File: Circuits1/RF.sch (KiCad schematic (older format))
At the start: 16 parts

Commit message: PCB Layout with 0806
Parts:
- removed X?: QUARTZCMS4, ~, symbol QUARTZCMS4
- added X2: QUARTZ, ~, symbol QUARTZ
- gave numbers to parts that had none: 15
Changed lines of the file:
@@
 LIBS:ATMEGA32U4
 LIBS:nRF24L01+
+LIBS:LD1117
+LIBS:MPU-6050
 LIBS:Rx-cache
 EELAYER 27 0
@@
 $Descr A4 11693 8268
 encoding utf-8
-Sheet 2 2
+Sheet 2 3
 Title "noname.sch"
-Date "16 dec 2013"
+Date "22 dec 2013"
 Rev ""
 Comp ""
@@
 $EndDescr
 $Comp
-L NRF24L01+ U?
+L NRF24L01+ U3
 U 1 1 52AF7B40
 P 5550 3550
-F 0 "U?" H 5550 3450 50  0000 C CNN
+F 0 "U3" H 5550 3450 50  0000 C CNN
 F 1 "NRF24L01+" H 5550 3650 50  0000 C CNN
 F 2 "MODULE" H 5550 3550 50  0001 C CNN
@@
 $EndComp
 $Comp
-L C C?
+L C C13
 U 1 1 52AF7B4F
 P 4300 2050
-F 0 "C?" H 4300 2150 40  0000 L CNN
+F 0 "C13" H 4300 2150 40  0000 L CNN
 F 1 "10nF" H 4306 1965 40  0000 L CNN
 F 2 "~" H 4338 1900 30  0000 C CNN
@@
 $EndComp
 $Comp
-L 3V3 #PWR?
+L 3V3 #PWR039
 U 1 1 52AF7B9D
 P 4400 2850
-F 0 "#PWR?" H 4400 2950 40  0001 C CNN
+F 0 "#PWR039" H 4400 2950 40  0001 C CNN
 F 1 "3V3" H 4400 2975 40  0000 C CNN
 F 2 "" H 4400 2850 60  0000 C CNN
@@
 $EndComp
 $Comp
-L 3V3 #PWR?
+L 3V3 #PWR040
 U 1 1 52AF7BC7
 P 4400 3300
-F 0 "#PWR?" H 4400 3400 40  0001 C CNN
+F 0 "#PWR040" H 4400 3400 40  0001 C CNN
 F 1 "3V3" H 4400 3425 40  0000 C CNN
 F 2 "" H 4400 3300 60  0000 C CNN
@@
 $EndComp
 $Comp
-L 3V3 #PWR?
+L 3V3 #PWR041
 U 1 1 52AF7BCD
 P 4400 3900
-F 0 "#PWR?" H 4400 4000 40  0001 C CNN
+F 0 "#PWR041" H 4400 4000 40  0001 C CNN
 F 1 "3V3" H 4400 4025 40  0000 C CNN
 F 2 "" H 4400 3900 60  0000 C CNN
@@
 $EndComp
 $Comp
-L GND #PWR?
+L GND #PWR042
 U 1 1 52AF7BF4
 P 4400 4250
-F 0 "#PWR?" H 4400 4250 30  0001 C CNN
+F 0 "#PWR042" H 4400 4250 30  0001 C CNN
 F 1 "GND" H 4400 4180 30  0001 C CNN
 F 2 "" H 4400 4250 60  0000 C CNN
@@
 $EndComp
 $Comp
-L GND #PWR?
+L GND #PWR043
 U 1 1 52AF7C01
 P 4400 3800
-F 0 "#PWR?" H 4400 3800 30  0001 C CNN
+F 0 "#PWR043" H 4400 3800 30  0001 C CNN
 F 1 "GND" H 4400 3730 30  0001 C CNN
 F 2 "" H 4400 3800 60  0000 C CNN
@@
 $EndComp
 $Comp
-L GND #PWR?
+L GND #PWR044
 U 1 1 52AF7C07
 P 4400 3200
-F 0 "#PWR?" H 4400 3200 30  0001 C CNN
+F 0 "#PWR044" H 4400 3200 30  0001 C CNN
 F 1 "GND" H 4400 3130 30  0001 C CNN
 F 2 "" H 4400 3200 60  0000 C CNN
@@
 $EndComp
 $Comp
-L GND #PWR?
+L GND #PWR045
 U 1 1 52AF7C0D
 P 4400 2950
-F 0 "#PWR?" H 4400 2950 30  0001 C CNN
+F 0 "#PWR045" H 4400 2950 30  0001 C CNN
 F 1 "GND" H 4400 2880 30  0001 C CNN
 F 2 "" H 4400 2950 60  0000 C CNN
@@
 $EndComp
 $Comp
-L R R?
+L R R8
 U 1 1 52AF7C2F
 P 4250 3550
-F 0 "R?" V 4330 3550 40  0000 C CNN
+F 0 "R8" V 4330 3550 40  0000 C CNN
 F 1 "22K" V 4257 3551 40  0000 C CNN
 F 2 "~" V 4180 3550 30  0000 C CNN
@@
 $EndComp
 $Comp
-L GND #PWR?
+L GND #PWR046
 U 1 1 52AF7C69
 P 3900 3550
-F 0 "#PWR?" H 3900 3550 30  0001 C CNN
+F 0 "#PWR046" H 3900 3550 30  0001 C CNN
 F 1 "GND" H 3900 3480 30  0001 C CNN
 F 2 "" H 3900 3550 60  0000 C CNN
@@
 $EndComp
 $Comp
-L C C?
+L C C14
 U 1 1 52AF7CD7
 P 4600 2050
-F 0 "C?" H 4600 2150 40  0000 L CNN
+F 0 "C14" H 4600 2150 40  0000 L CNN
 F 1 "1nF" H 4606 1965 40  0000 L CNN
 F 2 "~" H 4638 1900 30  0000 C CNN
@@
 $EndComp
 $Comp
-L 3V3 #PWR?
+L 3V3 #PWR047
 U 1 1 52AF7CEB
 P 4450 1700
-F 0 "#PWR?" H 4450 1800 40  0001 C CNN
+F 0 "#PWR047" H 4450 1800 40  0001 C CNN
 F 1 "3V3" H 4450 1825 40  0000 C CNN
 F 2 "" H 4450 1700 60  0000 C CNN
@@
 $EndComp
 $Comp
-L GND #PWR?
+L GND #PWR048
 U 1 1 52AF7D51
 P 4450 2350
-F 0 "#PWR?" H 4450 2350 30  0001 C CNN
+F 0 "#PWR048" H 4450 2350 30  0001 C CNN
 F 1 "GND" H 4450 2280 30  0001 C CNN
 F 2 "" H 4450 2350 60  0000 C CNN
@@
 3V3
 $Comp
-L QUARTZCMS4 X?
-U 1 1 52AF7E4F
-P 7250 3700
-F 0 "X?" H 7250 3850 60  0000 C CNN
-F 1 "QUARTZCMS4" H 7250 3550 60  0000 C CNN
-F 2 "~" H 7250 3700 60  0000 C CNN
-F 3 "~" H 7250 3700 60  0000 C CNN
-	1    7250 3700
-	0    -1   -1   0
-$EndComp
-$Comp
-L R R?
+L R R9
 U 1 1 52AF7E5E
 P 7600 3700
-F 0 "R?" V 7680 3700 40  0000 C CNN
+F 0 "R9" V 7680 3700 40  0000 C CNN
 F 1 "1M" V 7607 3701 40  0000 C CNN
 F 2 "~" V 7530 3700 30  0000 C CNN
@@
 $EndComp
 $Comp
-L C C?
+L C C16
 U 1 1 52AF7E77
 P 8000 3400
-F 0 "C?" H 8000 3500 40  0000 L CNN
+F 0 "C16" H 8000 3500 40  0000 L CNN
 F 1 "22pF" H 8006 3315 40  0000 L CNN
 F 2 "~" H 8038 3250 30  0000 C CNN
@@
 $EndComp
 $Comp
-L C C?
+L C C17
 U 1 1 52AF7E9C
 P 8000 4000
-F 0 "C?" H 8000 4100 40  0000 L CNN
+F 0 "C17" H 8000 4100 40  0000 L CNN
 F 1 "22pF" H 8006 3915 40  0000 L CNN
 F 2 "~" H 8038 3850 30  0000 C CNN
@@
 $EndComp
 $Comp
-L GND #PWR?
+L GND #PWR049
 U 1 1 52AF7F50
 P 8300 3400
-F 0 "#PWR?" H 8300 3400 30  0001 C CNN
+F 0 "#PWR049" H 8300 3400 30  0001 C CNN
 F 1 "GND" H 8300 3330 30  0001 C CNN
 F 2 "" H 8300 3400 60  0000 C CNN
@@
 $EndComp
 $Comp
-L GND #PWR?
+L GND #PWR050
 U 1 1 52AF7F6A
 P 8300 4000
-F 0 "#PWR?" H 8300 4000 30  0001 C CNN
+F 0 "#PWR050" H 8300 4000 30  0001 C CNN
 F 1 "GND" H 8300 3930 30  0001 C CNN
 F 2 "" H 8300 4000 60  0000 C CNN
@@
 $EndComp
 $Comp
-L INDUCTOR_SMALL L?
+L INDUCTOR_SMALL L1
 U 1 1 52AF7FBE
 P 6650 4600
-F 0 "L?" H 6650 4700 50  0000 C CNN
+F 0 "L1" H 6650 4700 50  0000 C CNN
 F 1 "8.2nH" H 6650 4550 50  0000 C CNN
 F 2 "~" H 6650 4600 60  0000 C CNN
@@
 $EndComp
 $Comp
-L INDUCTOR_SMALL L?
+L INDUCTOR_SMALL L2
 U 1 1 52AF7FDC
 P 7200 4850
-F 0 "L?" H 7200 4950 50  0000 C CNN
+F 0 "L2" H 7200 4950 50  0000 C CNN
 F 1 "3.9nH" H 7200 4800 50  0000 C CNN
 F 2 "~" H 7200 4850 60  0000 C CNN
@@
 $EndComp
 $Comp
-L INDUCTOR_SMALL L?
+L INDUCTOR_SMALL L3
 U 1 1 52AF7FEE
 P 7550 4350
-F 0 "L?" H 7550 4450 50  0000 C CNN
+F 0 "L3" H 7550 4450 50  0000 C CNN
 F 1 "2.7nH" H 7550 4300 50  0000 C CNN
 F 2 "~" H 7550 4350 60  0000 C CNN
@@
 $EndComp
 $Comp
-L C C?
+L C C20
 U 1 1 52AF8000
 P 8400 4400
-F 0 "C?" H 8400 4500 40  0000 L CNN
+F 0 "C20" H 8400 4500 40  0000 L CNN
 F 1 "2.2nF" H 8406 4315 40  0000 L CNN
 F 2 "~" H 8438 4250 30  0000 C CNN
@@
 $EndComp
 $Comp
-L C C?
+L C C18
 U 1 1 52AF8021
 P 8200 4400
-F 0 "C?" H 8200 4500 40  0000 L CNN
+F 0 "C18" H 8200 4500 40  0000 L CNN
 F 1 "4.7pF" H 8206 4315 40  0000 L CNN
 F 2 "~" H 8238 4250 30  0000 C CNN
@@
 $EndComp
 $Comp
-L GND #PWR?
+L GND #PWR051
 U 1 1 52AF8065
 P 8200 4700
-F 0 "#PWR?" H 8200 4700 30  0001 C CNN
+F 0 "#PWR051" H 8200 4700 30  0001 C CNN
 F 1 "GND" H 8200 4630 30  0001 C CNN
 F 2 "" H 8200 4700 60  0000 C CNN
@@
 $EndComp
 $Comp
-L GND #PWR?
+L GND #PWR052
 U 1 1 52AF806B
 P 8400 4700
-F 0 "#PWR?" H 8400 4700 30  0001 C CNN
+F 0 "#PWR052" H 8400 4700 30  0001 C CNN
 F 1 "GND" H 8400 4630 30  0001 C CNN
 F 2 "" H 8400 4700 60  0000 C CNN
@@
 $EndComp
 $Comp
-L C C?
+L C C15
 U 1 1 52AF8280
 P 7850 4850
-F 0 "C?" H 7850 4950 40  0000 L CNN
+F 0 "C15" H 7850 4950 40  0000 L CNN
 F 1 "1.5pF" H 7856 4765 40  0000 L CNN
 F 2 "~" H 7888 4700 30  0000 C CNN
@@
 $EndComp
 $Comp
-L C C?
+L C C19
 U 1 1 52AF8292
 P 8250 5050
-F 0 "C?" H 8250 5150 40  0000 L CNN
+F 0 "C19" H 8250 5150 40  0000 L CNN
 F 1 "1pF" H 8256 4965 40  0000 L CNN
 F 2 "~" H 8288 4900 30  0000 C CNN
@@
 $EndComp
 $Comp
-L GND #PWR?
+L GND #PWR053
 U 1 1 52AF8326
 P 8250 5400
-F 0 "#PWR?" H 8250 5400 30  0001 C CNN
+F 0 "#PWR053" H 8250 5400 30  0001 C CNN
 F 1 "GND" H 8250 5330 30  0001 C CNN
 F 2 "" H 8250 5400 60  0000 C CNN
@@
 ANTENNA
 $Comp
-L C C?
+L C C12
 U 1 1 52AF8407
 P 4250 4150
-F 0 "C?" H 4250 4250 40  0000 L CNN
+F 0 "C12" H 4250 4250 40  0000 L CNN
 F 1 "33nF" H 4256 4065 40  0000 L CNN
 F 2 "~" H 4288 4000 30  0000 C CNN
@@
 $EndComp
 $Comp
-L GND #PWR?
+L GND #PWR054
 U 1 1 52AF841C
 P 3950 4150
-F 0 "#PWR?" H 3950 4150 30  0001 C CNN
+F 0 "#PWR054" H 3950 4150 30  0001 C CNN
 F 1 "GND" H 3950 4080 30  0001 C CNN
 F 2 "" H 3950 4150 60  0000 C CNN
@@
 Wire Wire Line
 	4450 4150 4600 4150
+$Comp
+L QUARTZ X2
+U 1 1 52B08D5B
+P 7250 3700
+F 0 "X2" H 7250 3850 60  0000 C CNN
+F 1 "QUARTZ" H 7250 3550 60  0000 C CNN
+F 2 "~" H 7250 3700 60  0000 C CNN
+F 3 "~" H 7250 3700 60  0000 C CNN
+	1    7250 3700
+	0    -1   -1   0
+$EndComp
 $EndSCHEMATC

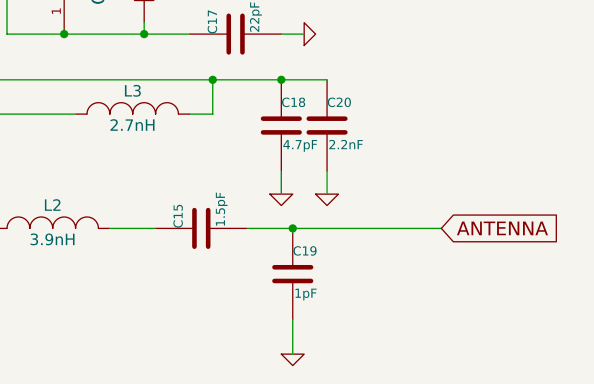
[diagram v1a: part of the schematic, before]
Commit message: Antenna and Ground Planes
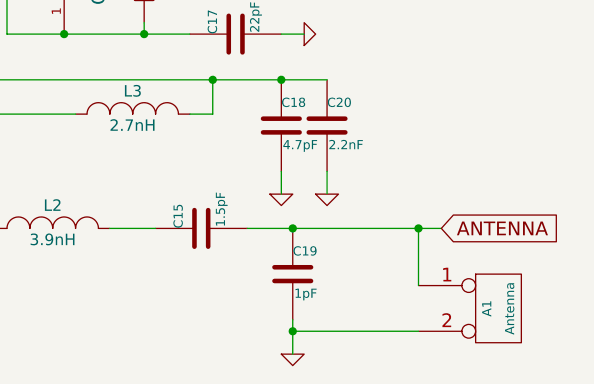
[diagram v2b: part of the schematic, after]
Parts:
- added A1: Antenna, symbol CONN_2
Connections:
- wire segments 46 -> 48
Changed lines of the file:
@@
 Sheet 2 3
 Title "noname.sch"
-Date "22 dec 2013"
+Date "23 dec 2013"
 Rev ""
 Comp ""
@@
 	0    -1   -1   0
 $EndComp
+$Comp
+L CONN_2 A1
+U 1 1 52B8818A
+P 9150 5200
+F 0 "A1" V 9100 5200 40  0000 C CNN
+F 1 "Antenna" V 9200 5200 40  0000 C CNN
+F 2 "" H 9150 5200 60  0000 C CNN
+F 3 "" H 9150 5200 60  0000 C CNN
+	1    9150 5200
+	1    0    0    -1
+$EndComp
+Wire Wire Line
+	8800 4850 8800 5100
+Connection ~ 8800 4850
+Wire Wire Line
+	8800 5300 8250 5300
+Connection ~ 8250 5300
 $EndSCHEMATC
